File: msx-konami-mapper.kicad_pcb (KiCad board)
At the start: 2 copper layers, 65.3 x 63 mm, 3 parts, among them U1 SST39SF040

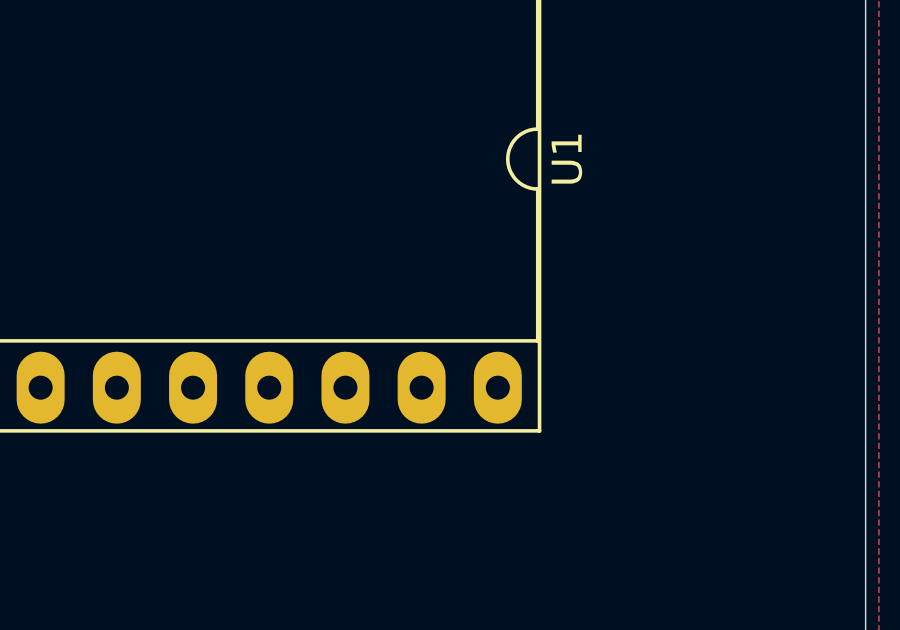
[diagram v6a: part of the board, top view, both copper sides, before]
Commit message: Disable programming for v1.0
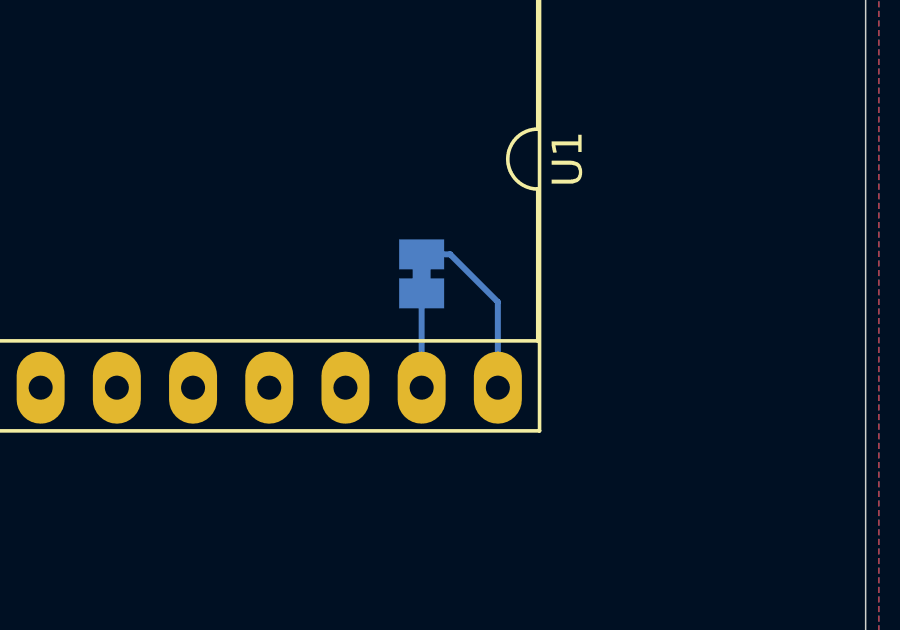
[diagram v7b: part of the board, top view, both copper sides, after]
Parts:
- added JP1: Jumper_2_Bridged, Jumper:SolderJumper-2_P1.3mm_Bridged_Pad1.0x1.5mm, B.Cu at (190.5, 76.2)
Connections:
- U1 pad 31: unconnected-(U1-PGM-Pad31) -> Net-(JP1-B)
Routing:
- net +5V: track 19.3 -> 25.3 mm
- net Net-(JP1-B): track 0.00 -> 3.15 mm
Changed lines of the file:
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@@
 	)
 	(net 0 "")
-	(net 1 "unconnected-(U1-PGM-Pad31)")
+	(net 1 "Net-(JP1-B)")
 	(net 2 "/D5")
 	(net 3 "/D6")
@@
 			(layers "*.Cu" "*.Mask")
 			(remove_unused_layers no)
-			(net 1 "unconnected-(U1-PGM-Pad31)")
+			(net 1 "Net-(JP1-B)")
 			(pinfunction "PGM")
 			(pintype "input")
@@
 		)
 	)
+	(footprint "Jumper:SolderJumper-2_P1.3mm_Bridged_Pad1.0x1.5mm"
+		(layer "B.Cu")
+		(at 190.5 76.215 -90)
+		(descr "SMD Solder Jumper, 1x1.5mm Pads, 0.3mm gap, bridged with 1 copper strip")
+		(tags "net tie solder jumper bridged")
+		(property "Reference" "JP1"
+			(at 0 1.8 90)
+			(layer "B.SilkS")
+			(effects
+				(font
+					(size 1 1)
+					(thickness 0.15)
+				)
+				(justify mirror)
+			)
+		)
+		(property "Value" "Jumper_2_Bridged"
+			(at 0 -1.9 90)
+			(layer "B.Fab")
+			(effects
+				(font
+					(size 1 1)
+					(thickness 0.15)
+				)
+				(justify mirror)
+			)
+		)
+		(property "Footprint" "Jumper:SolderJumper-2_P1.3mm_Bridged_Pad1.0x1.5mm"
+			(at 0 0 90)
+			(unlocked yes)
+			(layer "B.Fab")
+			(hide yes)
+			(effects
+				(font
+					(size 1.27 1.27)
+					(thickness 0.15)
+				)
+				(justify mirror)
+			)
+		)
+		(property "Datasheet" ""
+			(at 0 0 90)
+			(unlocked yes)
+			(layer "B.Fab")
+			(hide yes)
+			(effects
+				(font
+					(size 1.27 1.27)
+					(thickness 0.15)
+				)
+				(justify mirror)
+			)
+		)
+		(property "Description" "Jumper, 2-pole, closed/bridged"
+			(at 0 0 90)
+			(unlocked yes)
+			(layer "B.Fab")
+			(hide yes)
+			(effects
+				(font
+					(size 1.27 1.27)
+					(thickness 0.15)
+				)
+				(justify mirror)
+			)
+		)
+		(property ki_fp_filters "Jumper* TestPoint*2Pads* TestPoint*Bridge*")
+		(sheetname "Root")
+		(sheetfile "msx-konami-mapper.kicad_sch")
+		(zone_connect 1)
+		(attr exclude_from_pos_files)
+		(net_tie_pad_groups "1, 2")
+		(fp_poly
+			(pts
+				(xy -0.25 0.3) (xy 0.25 0.3) (xy 0.25 -0.3) (xy -0.25 -0.3)
+			)
+			(stroke
+				(width 0)
+				(type solid)
+			)
+			(fill solid)
+			(layer "B.Cu")
+		)
+		(fp_line
+			(start -1.4 1)
+			(end -1.4 -1)
+			(stroke
+				(width 0.12)
+				(type solid)
+			)
+			(layer "B.SilkS")
+		)
+		(fp_line
+			(start 1.4 1)
+			(end -1.4 1)
+			(stroke
+				(width 0.12)
+				(type solid)
+			)
+			(layer "B.SilkS")
+		)
+		(fp_line
+			(start -1.4 -1)
+			(end 1.4 -1)
+			(stroke
+				(width 0.12)
+				(type solid)
+			)
+			(layer "B.SilkS")
+		)
+		(fp_line
+			(start 1.4 -1)
+			(end 1.4 1)
+			(stroke
+				(width 0.12)
+				(type solid)
+			)
+			(layer "B.SilkS")
+		)
+		(fp_line
+			(start 1.65 1.25)
+			(end -1.65 1.25)
+			(stroke
+				(width 0.05)
+				(type solid)
+			)
+			(layer "B.CrtYd")
+		)
+		(fp_line
+			(start 1.65 1.25)
+			(end 1.65 -1.25)
+			(stroke
+				(width 0.05)
+				(type solid)
+			)
+			(layer "B.CrtYd")
+		)
+		(fp_line
+			(start -1.65 -1.25)
+			(end -1.65 1.25)
+			(stroke
+				(width 0.05)
+				(type solid)
+			)
+			(layer "B.CrtYd")
+		)
+		(fp_line
+			(start -1.65 -1.25)
+			(end 1.65 -1.25)
+			(stroke
+				(width 0.05)
+				(type solid)
+			)
+			(layer "B.CrtYd")
+		)
+		(pad "1" smd rect
+			(at -0.65 0 270)
+			(size 1 1.5)
+			(layers "B.Cu" "B.Mask")
+			(net 48 "+5V")
+			(pinfunction "A")
+			(pintype "passive")
+		)
+		(pad "2" smd rect
+			(at 0.65 0 270)
+			(size 1 1.5)
+			(layers "B.Cu" "B.Mask")
+			(net 1 "Net-(JP1-B)")
+			(pinfunction "B")
+			(pintype "passive")
+		)
+	)
 	(gr_poly
 		(pts
@@
 	)
 	(segment
+		(start 190.5 80.01)
+		(end 190.5 76.865)
+		(width 0.2)
+		(layer "B.Cu")
+		(net 1)
+	)
+	(segment
 		(start 154.94 102.87)
 		(end 156.21 101.6)
@@
 	)
 	(segment
+		(start 190.5 75.565)
+		(end 191.45 75.565)
+		(width 0.2)
+		(layer "B.Cu")
+		(net 48)
+	)
+	(segment
 		(start 144.78 100.584)
 		(end 144.78 101.346)
@@
 	)
 	(segment
+		(start 191.45 75.565)
+		(end 193.04 77.155)
+		(width 0.2)
+		(layer "B.Cu")
+		(net 48)
+	)
+	(segment
 		(start 146.431 99.695)
 		(end 145.669 99.695)
@@
 		(layer "B.Cu")
 		(net 48)
+	)
+	(segment
+		(start 193.04 77.155)
+		(end 193.04 80.01)
+		(width 0.2)
+		(layer "B.Cu")
+		(net 48)

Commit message: Experimental dual-game select
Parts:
- added SW1: High/Low, Connector_PinHeader_2.54mm:PinHeader_1x03_P2.54mm_Vertical, F.Cu at (200.7, 71.8)
- added U3: 74LS670, Package_DIP:DIP-16_W7.62mm_Socket_LongPads, F.Cu at (175.3, 95.2)
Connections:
- U1 pad 1: unconnected-(U1-A18-Pad1) -> /PA18
- U1 pad 10: unconnected-(U1-A2-Pad10) -> /A2
- U1 pad 11: unconnected-(U1-A1-Pad11) -> /A1
- U1 pad 12: unconnected-(U1-A0-Pad12) -> /A0
- U1 pad 2: unconnected-(U1-A16-Pad2) -> /PA16
- U1 pad 23: unconnected-(U1-A10-Pad23) -> /A10
- U1 pad 25: unconnected-(U1-A11-Pad25) -> /A11
- U1 pad 26: unconnected-(U1-A9-Pad26) -> /A9
- U1 pad 27: unconnected-(U1-A8-Pad27) -> /A8
- U1 pad 28: unconnected-(U1-A13-Pad28) -> /PA13
- U1 pad 29: unconnected-(U1-A14-Pad29) -> /PA14
- U1 pad 3: unconnected-(U1-A15-Pad3) -> /PA15
- U1 pad 30: unconnected-(U1-A17-Pad30) -> /PA17
- U1 pad 4: unconnected-(U1-A12-Pad4) -> /A12
- U1 pad 5: unconnected-(U1-A7-Pad5) -> /A7
- U1 pad 6: unconnected-(U1-A6-Pad6) -> /A6
- U1 pad 7: unconnected-(U1-A5-Pad7) -> /A5
- U1 pad 8: unconnected-(U1-A4-Pad8) -> /A4
- U1 pad 9: unconnected-(U1-A3-Pad9) -> /A3
- U2 pad 17: unconnected-(U2-A9-Pad17) -> /A9
- U2 pad 19: unconnected-(U2-A11-Pad19) -> /A11
- U2 pad 20: unconnected-(U2-A10-Pad20) -> /A10
- U2 pad 21: unconnected-(U2-A7-Pad21) -> /A7
- U2 pad 22: unconnected-(U2-A6-Pad22) -> /A6
- U2 pad 23: unconnected-(U2-A12-Pad23) -> /A12
- U2 pad 24: unconnected-(U2-A8-Pad24) -> /A8
- U2 pad 26: unconnected-(U2-A13-Pad26) -> /A13
- U2 pad 27: unconnected-(U2-A1-Pad27) -> /A1
- U2 pad 28: unconnected-(U2-A0-Pad28) -> /A0
- U2 pad 29: unconnected-(U2-A3-Pad29) -> /A3
- U2 pad 30: unconnected-(U2-A2-Pad30) -> /A2
- U2 pad 31: unconnected-(U2-A5-Pad31) -> /A5
- U2 pad 32: unconnected-(U2-A4-Pad32) -> /A4
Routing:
- net /PA18: track 0.00 -> 12.1 mm, vias 0 -> 1
